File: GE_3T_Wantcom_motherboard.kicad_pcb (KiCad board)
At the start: 2 copper layers, 49.8 x 17.2 mm, 25 parts, among them J1 Conn_01x03

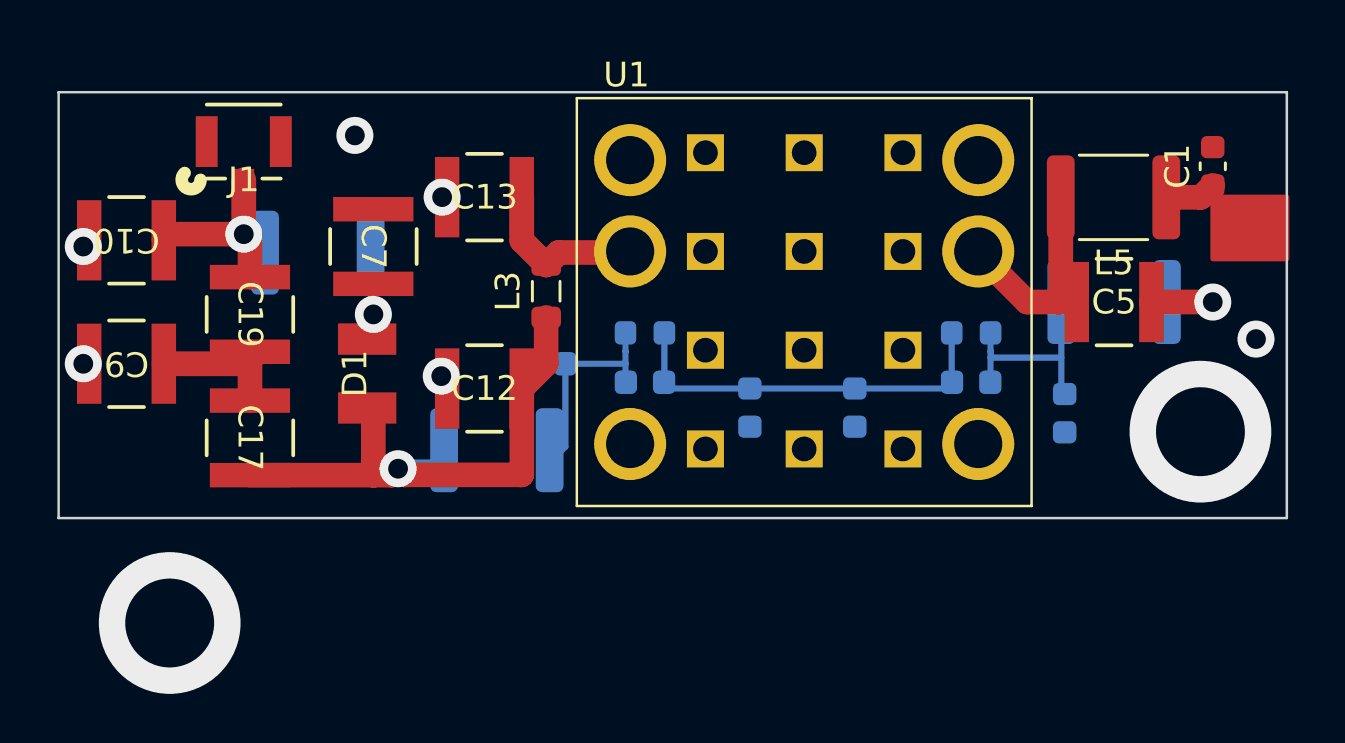
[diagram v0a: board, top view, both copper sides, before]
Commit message: board with screws, silkscreen issues
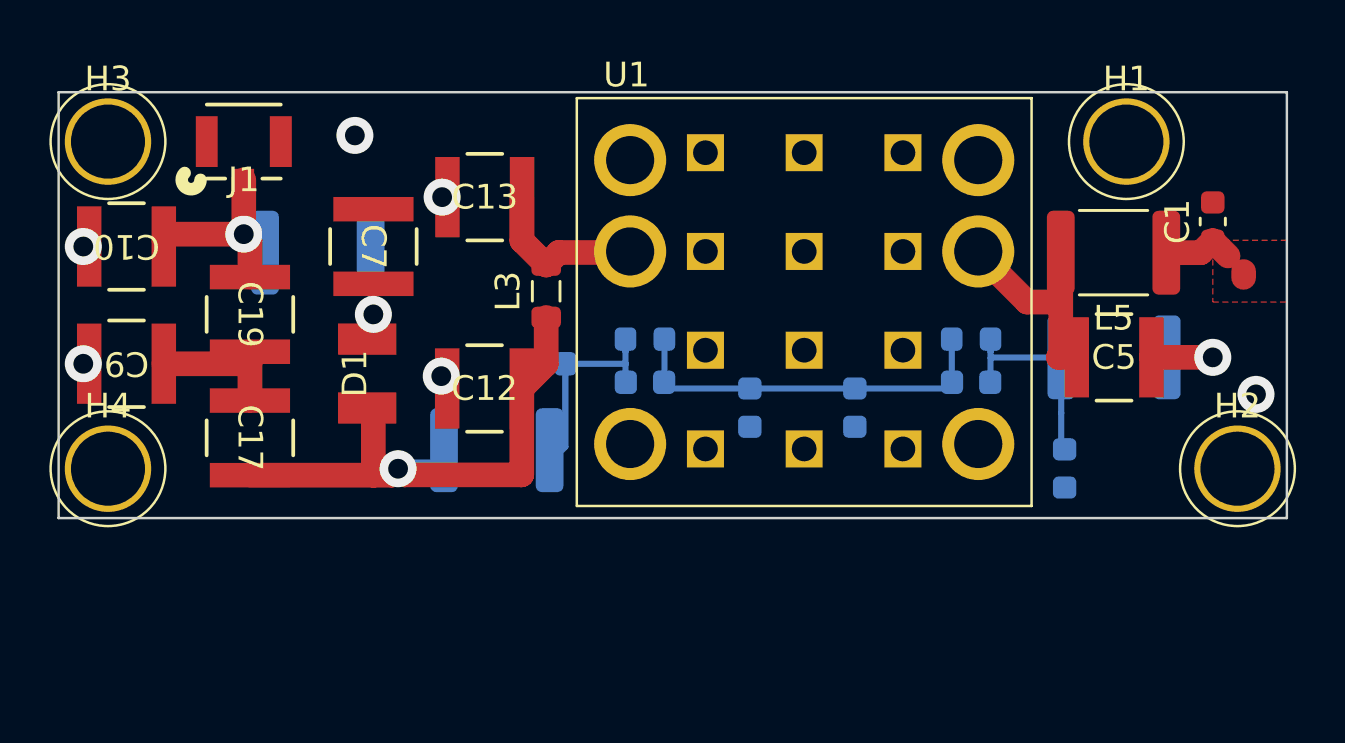
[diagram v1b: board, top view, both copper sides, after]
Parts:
- added H1: MountingHole, aaa_MyLib:screw head 440, F.Cu at (198.5, 102.0)
- added H2: MountingHole, aaa_MyLib:screw head 440, F.Cu at (203.0, 115.2)
- added H3: MountingHole, aaa_MyLib:screw head 440, F.Cu at (157.2, 102.0)
- added H4: MountingHole, aaa_MyLib:screw head 440, F.Cu at (157.2, 115.2)
- J1: footprint aaa_MyLib:CONN1_UFL-R_HIR -> aaa_UFL:CONN1_UFL-R_HIR
- moved C1 2.24 mm to (202.0, 105.2)
- moved C15 2.24 mm to (196.0, 115.2)
- moved C5 2.24 mm to (198.0, 110.7)
- moved L2 2.24 mm to (198.0, 110.7)
- moved L5 2.24 mm to (198.0, 106.5)
- moved C10 0.25 mm to (158.0, 106.2)
- moved L6 0.25 mm to (179.0, 110.0)
- moved L7 0.25 mm to (192.2, 110.0)
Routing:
- net +VDC: track 2.08 -> 3.19 mm
- net GND: vias 8 -> 6
- added copper zone on F.Cu, net +VDC

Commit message: board with screws better placement, silkscreen issues
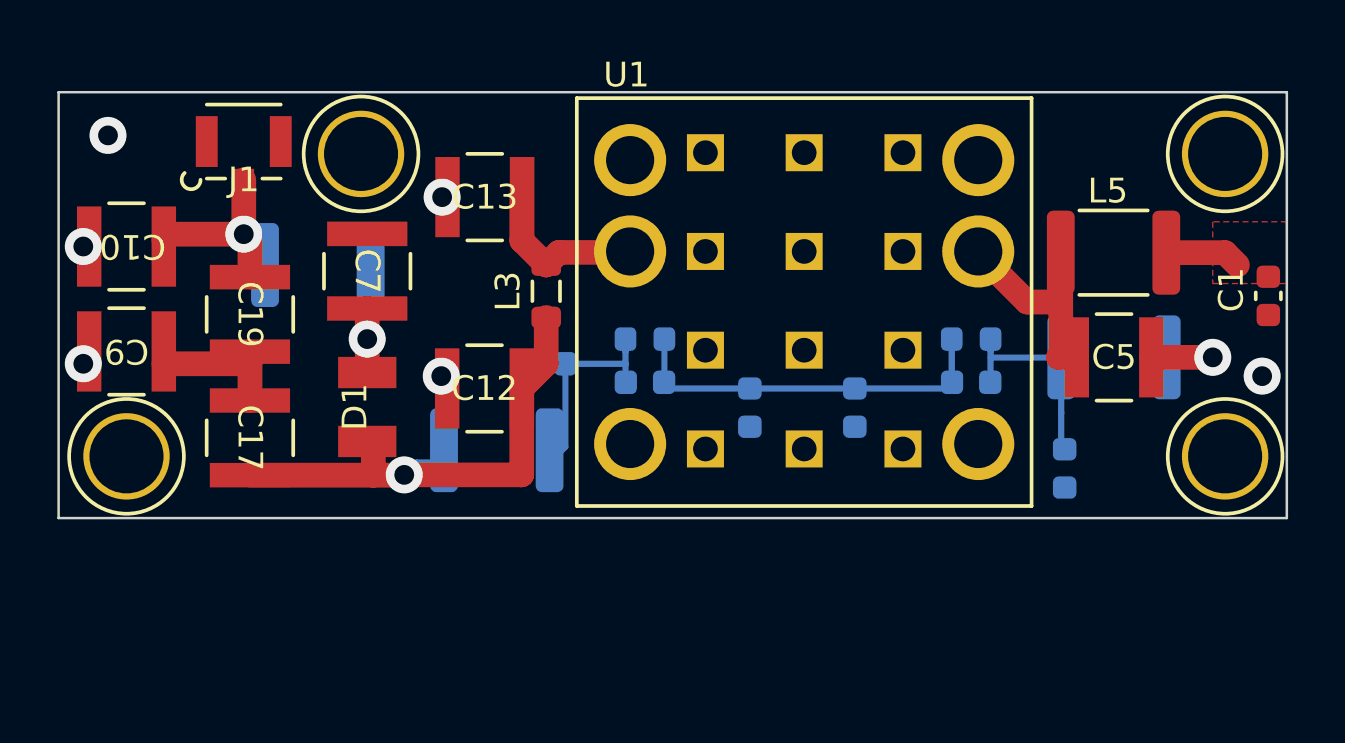
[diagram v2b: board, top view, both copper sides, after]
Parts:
- removed H1, H2, H3, H4: MountingHole, aaa_MyLib:screw head 440
- added J2: mounting screw, aaa_MyLib:screw head 440, F.Cu at (202.5, 114.8)
- added J3: mounting screw, aaa_MyLib:screw head 440, F.Cu at (202.5, 102.5)
- added J4: mounting screw, aaa_MyLib:screw head 440, F.Cu at (158.0, 114.8)
- added J5: mounting screw, aaa_MyLib:screw head 440, F.Cu at (167.5, 102.5)
- moved C1 3.76 mm to (204.2, 108.2), turned to -90 degrees
- moved D1 1.36 mm to (167.8, 112.8)
- moved C7 1.03 mm to (167.8, 107.2)
- moved C9 0.50 mm to (158.0, 110.5)
- moved L1 0.50 mm to (165.8, 107.0)
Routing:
- net Net-(D1-K): track 3.30 -> 5.40 mm
- net Net-(D1-A): track 22.1 -> 21.1 mm
